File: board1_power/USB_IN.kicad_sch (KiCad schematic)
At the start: 10 parts, among them J3 USB_C_Receptacle_USB2.0_16P, U11 USBLC6-2SC6, U12 CH224K

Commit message: board1_power: SYS-default channel rework + ESP32-S3 + mux + connectors
Channel (charge_chanel.kicad_sch):
- Reverse-polarity P-FET (DMG2305UX) moved to cell terminal, drain-to-battery;
  charger BAT on CELL_P_PROT, DW01A sense stays on raw CELL_P.
- 0R source selector (R_SYS populated / R_LOAD DNP, both 2010) -> CHn_V_pre,
  PTC relocated after it -> CH_V output. Old Q2/Q3 reverse FETs removed.
- Bootstrap cap 47nF, PMID 6.8uF. Per-cell SK6812 RGB on LED_VDD=CH1_V chain.

Root (board1_power.kicad_sch):
- ESP32-C3 -> ESP32-S3-WROOM-1. SDA=IO8, SCL=IO9, MUX_RST=IO10(+TCA9548A RESET),
  RGB_DATA=IO48 via 330R, USB=IO19/20, boot IO0=pull-up+JP1, heartbeat=IO2.
- Fixed IO45 strapping pin (was tied to +3V3 -> would force 1.8V flash; now NC).
- TCA9548A mux with per-channel I2C (CH1..4_SDA/SCL). 4.7k pull-ups on main bus.
- J2 power 8-pin (CH1..4_V + GND) and J3 signal 4-pin (SDA/SCL/CH_LIVE/SGND),
  both per interconnect.md.

Library: added DMG2305UX (P-FET, SOT-23) to libs/BMS.kicad_sym.

WIP remaining: PWR_FLAGs, no-connect on last RGB DOUT, drop stray CH3_GND label,
cell holders (CELL_P/N left floating by design), optional TPS22917 ESP gate.

Co-Authored-By: Claude Opus 4.8 (1M context) <noreply@anthropic.com>
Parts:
- renumbered C7 to C8, C8 to C9, D6 to D2, R5 to R11, R7 to R12, R10 to R13, R11 to R14, U11 to U4, U12 to U5
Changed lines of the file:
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@@
+	)
+	(junction
+		(at 130.175 47.625)
+		(diameter 0)
+		(color 0 0 0 0)
 	)
 	(junction
@@
 	(wire
 		(pts
-			(xy 123.825 47.625) (xy 131.445 47.625)
+			(xy 123.825 47.625) (xy 130.175 47.625)
 		)
 		(stroke
@@
 		(pts
 			(xy 201.93 58.42) (xy 201.93 59.69)
+		)
+		(stroke
+			(width 0)
+			(type default)
+		)
+	)
+	(wire
+		(pts
+			(xy 130.175 47.625) (xy 131.445 47.625)
 		)
 		(stroke
@@
 		(dnp no)
 		(fields_autoplaced yes)
-		(property "Reference" "U12"
+		(property "Reference" "U5"
 			(at 181.61 50.8 0)
 			(show_name no)
@@
 			(project "board1_power"
 				(path "/0d1390b9-e848-4ad4-8bef-84851d0f73a3/98574bda-0736-4dde-adc3-a95faa234ebf"
-					(reference "U12")
+					(reference "U5")
 					(unit 1)
 				)
@@
 		(dnp no)
 		(fields_autoplaced yes)
-		(property "Reference" "#PWR072"
+		(property "Reference" "#PWR036"
 			(at 180.34 125.095 0)
 			(hide yes)
@@
 			(project "board1_power"
 				(path "/0d1390b9-e848-4ad4-8bef-84851d0f73a3/98574bda-0736-4dde-adc3-a95faa234ebf"
-					(reference "#PWR072")
+					(reference "#PWR036")
 					(unit 1)
 				)
@@
 		(dnp no)
 		(fields_autoplaced yes)
-		(property "Reference" "#PWR026"
+		(property "Reference" "#PWR032"
 			(at 108.585 97.155 0)
 			(hide yes)
@@
 			(project "board1_power"
 				(path "/0d1390b9-e848-4ad4-8bef-84851d0f73a3/98574bda-0736-4dde-adc3-a95faa234ebf"
-					(reference "#PWR026")
+					(reference "#PWR032")
 					(unit 1)
 				)
@@
 		(dnp no)
 		(fields_autoplaced yes)
-		(property "Reference" "U11"
+		(property "Reference" "U4"
 			(at 108.3311 119.38 0)
 			(show_name no)
@@
 			(project "board1_power"
 				(path "/0d1390b9-e848-4ad4-8bef-84851d0f73a3/98574bda-0736-4dde-adc3-a95faa234ebf"
-					(reference "U11")
+					(reference "U4")
 					(unit 1)
 				)
@@
 		(dnp no)
 		(fields_autoplaced yes)
-		(property "Reference" "C7"
+		(property "Reference" "C8"
 			(at 184.15 125.4759 0)
 			(show_name no)
@@
 			(project "board1_power"
 				(path "/0d1390b9-e848-4ad4-8bef-84851d0f73a3/98574bda-0736-4dde-adc3-a95faa234ebf"
-					(reference "C7")
+					(reference "C8")
 					(unit 1)
 				)
@@
 		(dnp no)
 		(fields_autoplaced yes)
-		(property "Reference" "R11"
+		(property "Reference" "R14"
 			(at 222.25 62.2299 0)
 			(show_name no)
@@
 			(project "board1_power"
 				(path "/0d1390b9-e848-4ad4-8bef-84851d0f73a3/98574bda-0736-4dde-adc3-a95faa234ebf"
-					(reference "R11")
+					(reference "R14")
 					(unit 1)
 				)
@@
 		(dnp no)
 		(fields_autoplaced yes)
-		(property "Reference" "#PWR075"
+		(property "Reference" "#PWR039"
 			(at 198.12 50.8 0)
 			(hide yes)
@@
 			(project "board1_power"
 				(path "/0d1390b9-e848-4ad4-8bef-84851d0f73a3/98574bda-0736-4dde-adc3-a95faa234ebf"
-					(reference "#PWR075")
+					(reference "#PWR039")
 					(unit 1)
 				)
@@
 		(dnp no)
 		(fields_autoplaced yes)
-		(property "Reference" "R5"
+		(property "Reference" "R11"
 			(at 167.005 52.0699 0)
 			(show_name no)
@@
 			(project "board1_power"
 				(path "/0d1390b9-e848-4ad4-8bef-84851d0f73a3/98574bda-0736-4dde-adc3-a95faa234ebf"
-					(reference "R5")
+					(reference "R11")
 					(unit 1)
 				)
@@
 		(dnp no)
 		(fields_autoplaced yes)
-		(property "Reference" "#PWR074"
+		(property "Reference" "#PWR038"
 			(at 201.93 80.01 0)
 			(hide yes)
@@
 			(project "board1_power"
 				(path "/0d1390b9-e848-4ad4-8bef-84851d0f73a3/98574bda-0736-4dde-adc3-a95faa234ebf"
-					(reference "#PWR074")
+					(reference "#PWR038")
 					(unit 1)
 				)
@@
 		(dnp no)
 		(fields_autoplaced yes)
-		(property "Reference" "#PWR016"
+		(property "Reference" "#PWR029"
 			(at 100.965 97.155 0)
 			(hide yes)
@@
 			(project "board1_power"
 				(path "/0d1390b9-e848-4ad4-8bef-84851d0f73a3/98574bda-0736-4dde-adc3-a95faa234ebf"
-					(reference "#PWR016")
+					(reference "#PWR029")
 					(unit 1)
 				)
@@
 		(dnp no)
 		(fields_autoplaced yes)
-		(property "Reference" "R10"
+		(property "Reference" "R13"
 			(at 203.835 62.2299 0)
 			(show_name no)
@@
 			(project "board1_power"
 				(path "/0d1390b9-e848-4ad4-8bef-84851d0f73a3/98574bda-0736-4dde-adc3-a95faa234ebf"
-					(reference "R10")
+					(reference "R13")
 					(unit 1)
 				)
@@
 		(in_pos_files yes)
 		(dnp no)
-		(property "Reference" "R7"
+		(property "Reference" "R12"
 			(at 196.215 52.0699 0)
 			(show_name no)
@@
 			(project "board1_power"
 				(path "/0d1390b9-e848-4ad4-8bef-84851d0f73a3/98574bda-0736-4dde-adc3-a95faa234ebf"
-					(reference "R7")
+					(reference "R12")
 					(unit 1)
 				)
@@
 		(dnp no)
 		(fields_autoplaced yes)
-		(property "Reference" "#PWR024"
+		(property "Reference" "#PWR031"
 			(at 106.68 143.51 0)
 			(hide yes)
@@
 			(project "board1_power"
 				(path "/0d1390b9-e848-4ad4-8bef-84851d0f73a3/98574bda-0736-4dde-adc3-a95faa234ebf"
-					(reference "#PWR024")
+					(reference "#PWR031")
+					(unit 1)
+				)
+			)
+		)
+	)
+	(symbol
+		(lib_id "power:PWR_FLAG")
+		(at 130.175 47.625 0)
+		(unit 1)
+		(body_style 1)
+		(exclude_from_sim no)
+		(in_bom yes)
+		(on_board yes)
+		(in_pos_files yes)
+		(dnp no)
+		(fields_autoplaced yes)
+		(property "Reference" "#FLG06"
+			(at 130.175 45.72 0)
+			(hide yes)
+			(show_name no)
+			(do_not_autoplace no)
+			(effects
+				(font
+					(size 1.27 1.27)
+				)
+			)
+		)
+		(property "Value" "PWR_FLAG"
+			(at 130.175 42.545 0)
+			(show_name no)
+			(do_not_autoplace no)
+			(effects
+				(font
+					(size 1.27 1.27)
+				)
+			)
+		)
+		(property "Footprint" ""
+			(at 130.175 47.625 0)
+			(hide yes)
+			(show_name no)
+			(do_not_autoplace no)
+			(effects
+				(font
+					(size 1.27 1.27)
+				)
+			)
+		)
+		(property "Datasheet" ""
+			(at 130.175 47.625 0)
+			(hide yes)
+			(show_name no)
+			(do_not_autoplace no)
+			(effects
+				(font
+					(size 1.27 1.27)
+				)
+			)
+		)
+		(property "Description" "Special symbol for telling ERC where power comes from"
+			(at 130.175 47.625 0)
+			(hide yes)
+			(show_name no)
+			(do_not_autoplace no)
+			(effects
+				(font
+					(size 1.27 1.27)
+				)
+			)
+		)
+		(pin "1"
+		)
+		(instances
+			(project "board1_power"
+				(path "/0d1390b9-e848-4ad4-8bef-84851d0f73a3/98574bda-0736-4dde-adc3-a95faa234ebf"
+					(reference "#FLG06")
 					(unit 1)
 				)
@@
 		(dnp no)
 		(fields_autoplaced yes)
-		(property "Reference" "#PWR070"
+		(property "Reference" "#PWR034"
 			(at 164.465 41.91 0)
 			(hide yes)
@@
 			(project "board1_power"
 				(path "/0d1390b9-e848-4ad4-8bef-84851d0f73a3/98574bda-0736-4dde-adc3-a95faa234ebf"
-					(reference "#PWR070")
+					(reference "#PWR034")
 					(unit 1)
 				)
@@
 		(dnp no)
 		(fields_autoplaced yes)
-		(property "Reference" "D6"
+		(property "Reference" "D2"
 			(at 212.7885 61.595 0)
 			(show_name no)
@@
 			(project "board1_power"
 				(path "/0d1390b9-e848-4ad4-8bef-84851d0f73a3/98574bda-0736-4dde-adc3-a95faa234ebf"
-					(reference "D6")
+					(reference "D2")
 					(unit 1)
 				)
@@
 		(dnp no)
 		(fields_autoplaced yes)
-		(property "Reference" "#PWR076"
+		(property "Reference" "#PWR040"
 			(at 205.74 40.64 0)
 			(hide yes)
@@
 			(project "board1_power"
 				(path "/0d1390b9-e848-4ad4-8bef-84851d0f73a3/98574bda-0736-4dde-adc3-a95faa234ebf"
-					(reference "#PWR076")
+					(reference "#PWR040")
 					(unit 1)
 				)
@@
 		(dnp no)
 		(fields_autoplaced yes)
-		(property "Reference" "#PWR073"
+		(property "Reference" "#PWR037"
 			(at 180.34 140.335 0)
 			(hide yes)
@@
 			(project "board1_power"
 				(path "/0d1390b9-e848-4ad4-8bef-84851d0f73a3/98574bda-0736-4dde-adc3-a95faa234ebf"
-					(reference "#PWR073")
+					(reference "#PWR037")
 					(unit 1)
 				)
@@
 		(dnp no)
 		(fields_autoplaced yes)
-		(property "Reference" "#PWR017"
+		(property "Reference" "#PWR030"
 			(at 106.68 122.555 0)
 			(hide yes)
@@
 			(project "board1_power"
 				(path "/0d1390b9-e848-4ad4-8bef-84851d0f73a3/98574bda-0736-4dde-adc3-a95faa234ebf"
-					(reference "#PWR017")
+					(reference "#PWR030")
 					(unit 1)
 				)
@@
 		(dnp no)
 		(fields_autoplaced yes)
-		(property "Reference" "#PWR069"
+		(property "Reference" "#PWR033"
 			(at 127.635 47.625 0)
 			(hide yes)
@@
 			(project "board1_power"
 				(path "/0d1390b9-e848-4ad4-8bef-84851d0f73a3/98574bda-0736-4dde-adc3-a95faa234ebf"
-					(reference "#PWR069")
+					(reference "#PWR033")
 					(unit 1)
 				)
@@
 		(dnp no)
 		(fields_autoplaced yes)
-		(property "Reference" "C8"
+		(property "Reference" "C9"
 			(at 209.55 52.0699 0)
 			(show_name no)
@@
 			(project "board1_power"
 				(path "/0d1390b9-e848-4ad4-8bef-84851d0f73a3/98574bda-0736-4dde-adc3-a95faa234ebf"
-					(reference "C8")
+					(reference "C9")
 					(unit 1)
 				)
@@
 		(dnp no)
 		(fields_autoplaced yes)
-		(property "Reference" "#PWR071"
+		(property "Reference" "#PWR035"
 			(at 170.815 74.93 0)
 			(hide yes)
@@
 			(project "board1_power"
 				(path "/0d1390b9-e848-4ad4-8bef-84851d0f73a3/98574bda-0736-4dde-adc3-a95faa234ebf"
-					(reference "#PWR071")
+					(reference "#PWR035")
 					(unit 1)
 				)

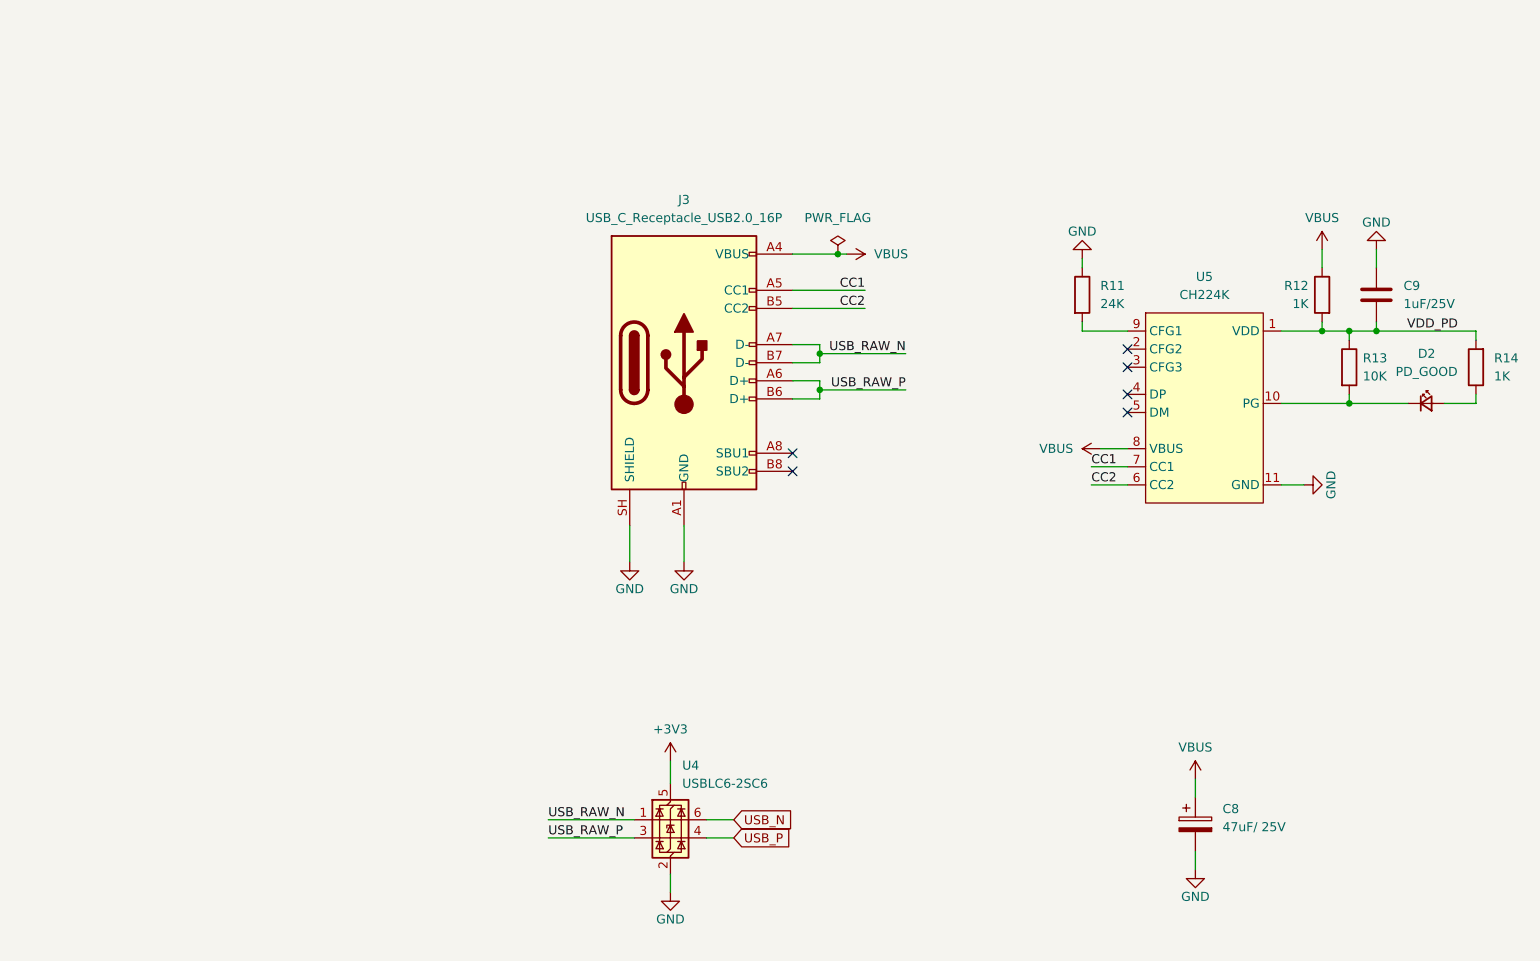
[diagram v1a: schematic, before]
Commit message: board1_power: enable network corrected + all footprints assigned (schematic complete)
- ESP enable rebuilt as a proper diode-OR + shunt:
  * MMBD4448HCQW (D12) quad common-cathode diode-OR -> EN, sources =
    {VBUS divider, CH1_V always-on strap (R59 now 100k), WAKE via 10k, self-hold}
  * R60 100k pull-down on EN (default off)
  * Q9 (2N7002) shunt: Drain->EN, Source->GND, Gate->off-header J4 (CH1_V when in)
  * off-header in -> ESP off (storage); out -> ESP on (launch)
- Assigned footprints to the remaining 26 parts (R/C -> 0603, D1 LED, J2 signal
  connector placeholder); channel-sheet parts apply across all 4 instances.

Remaining ERC items are benign/intentional (Unspecified-pin warnings from imported
symbols, floating cell pins until holder, missing PWR_FLAGs/no-connects).

Co-Authored-By: Claude Opus 4.8 (1M context) <noreply@anthropic.com>
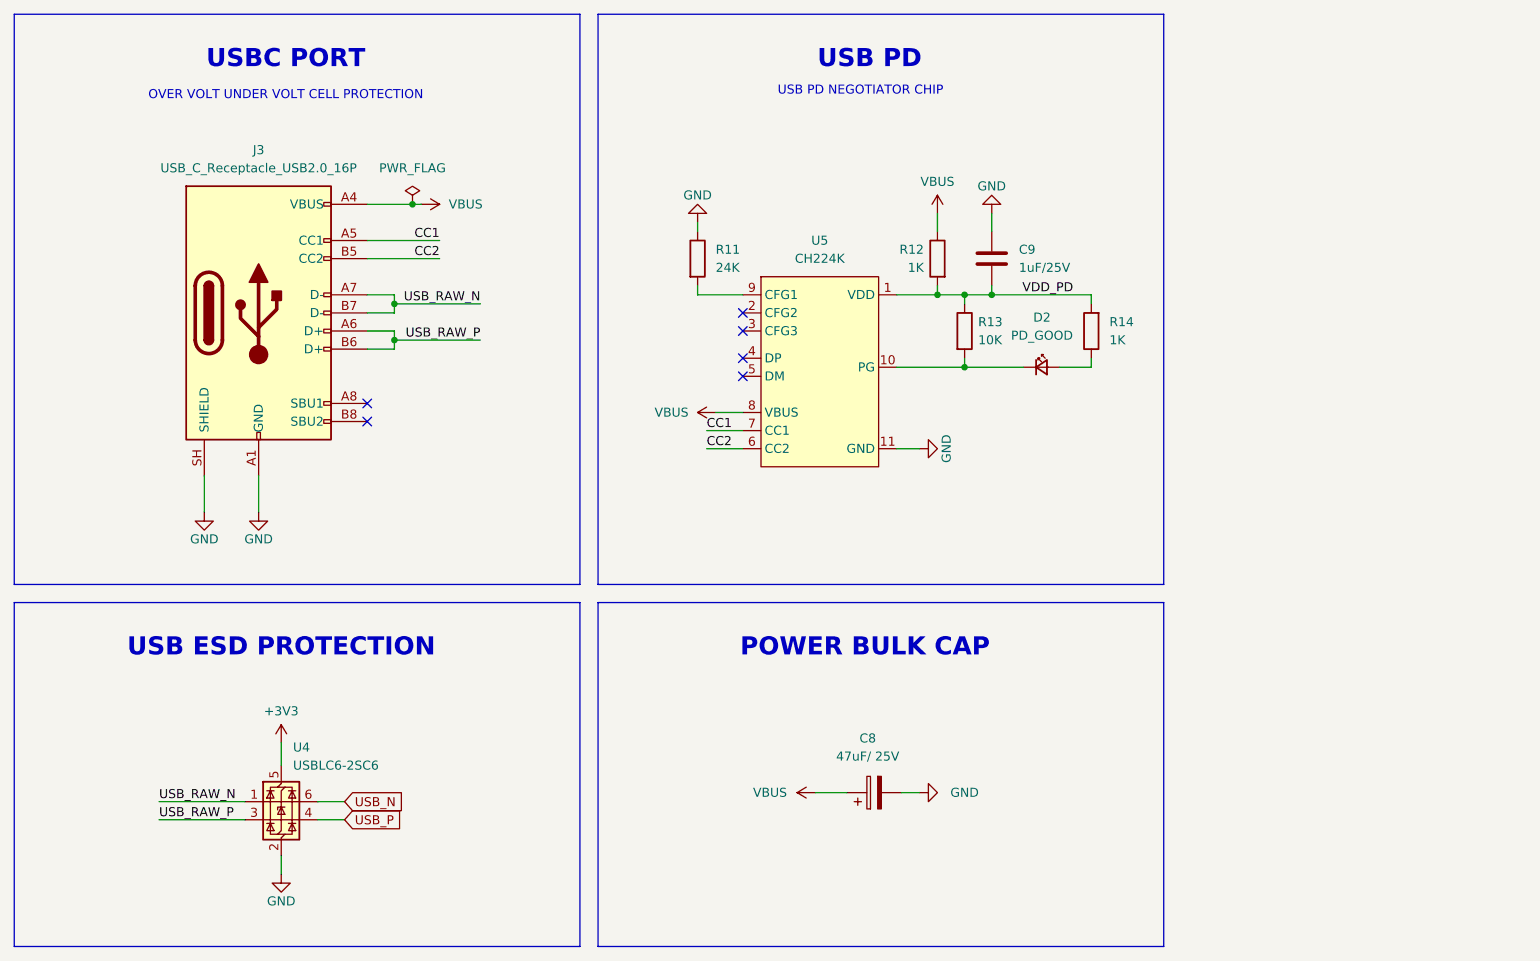
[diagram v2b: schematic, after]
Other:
- note added: "OVER VOLT UNDER VOLT CELL PROTECTION"
- note added: "POWER BULK CAP"
- note added: "USB ESD PROTECTION"
- note added: "USB PD"
- note added: "USB PD NEGOTIATOR CHIP"
- note added: "USBC PORT"
- moved on the sheet: C8, C9, D2, J3, R11, R12, R13, R14, U4, U5
